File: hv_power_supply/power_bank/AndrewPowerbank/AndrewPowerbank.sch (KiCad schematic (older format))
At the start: 49 parts, among them J1 NanoFit_RA_TH_02, J2 NanoFit_RA_TH_02, J3 USB-A-S-X-X-SM2, J4 USB-Micro-1981568-1, J5 NanoFit_RA_TH_02, Q1 SSM3K333R, U1 MCP73871T-2CCI_ML, U2 TPS61090RSAR

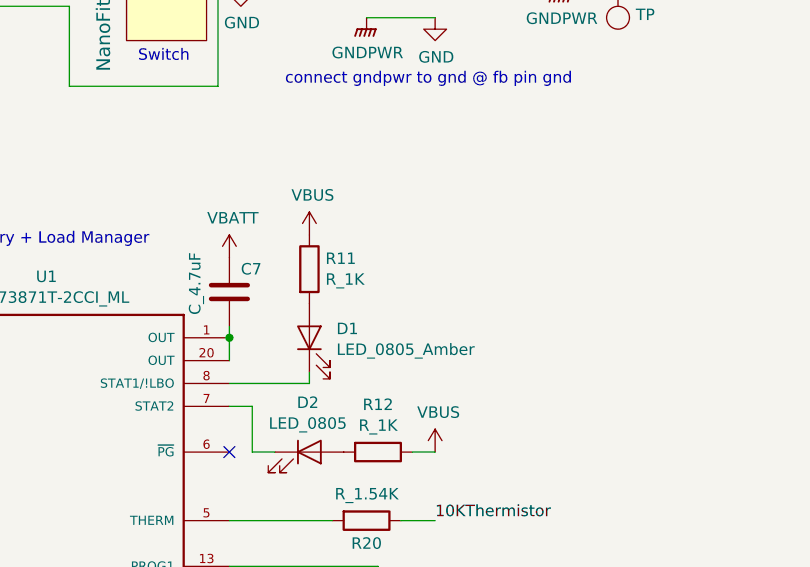
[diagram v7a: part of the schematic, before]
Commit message: Refill GND plane, fix C7 connection.
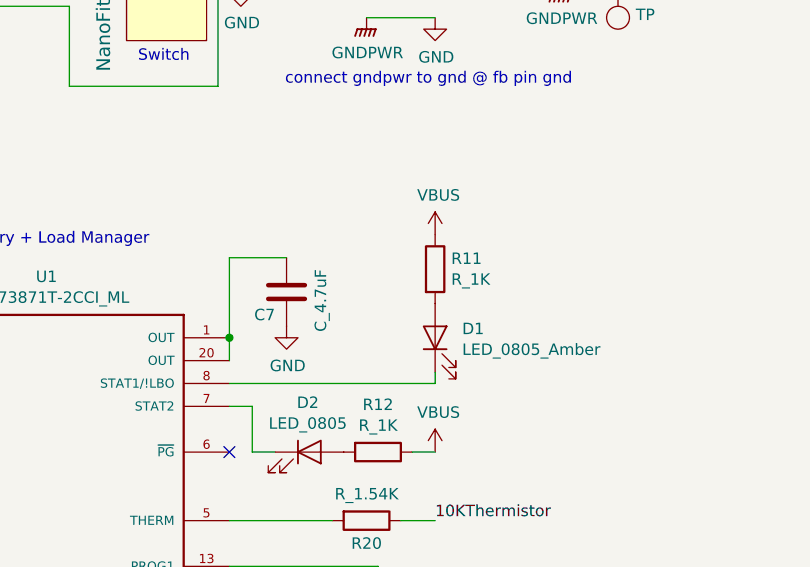
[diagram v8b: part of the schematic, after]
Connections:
- net +BATT: no longer C7.2
- net GND: now also C7.2
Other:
- moved on the sheet: C7, D1, R11
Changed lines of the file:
@@
 L formula:LED_0805_Amber D1
 U 1 1 5FD0F03B
-P 5950 4900
-F 0 "D1" V 5989 4782 50  0000 R CNN
-F 1 "LED_0805_Amber" V 5898 4782 50  0000 R CNN
-F 2 "footprints:LED_0805_OEM" H 5850 4900 50  0001 C CNN
-F 3 "https://media.digikey.com/pdf/Data%20Sheets/Chicago%20Miniature%20Lamps%20PDFs/CMDA5_Series_Rev_Aug_2014.pdf" H 5950 5000 50  0001 C CNN
-F 4 "DK" H 5950 4900 60  0001 C CNN "MFN"
-F 5 "L71517CT-ND" H 5950 4900 60  0001 C CNN "MPN"
-F 6 "https://www.digikey.com/product-detail/en/visual-communications-company-vcc/CMDA5DY7D1S/L71517CT-ND/614867" H 6350 5400 60  0001 C CNN "PurchasingLink"
-	1    5950 4900
+P 6500 4900
+F 0 "D1" V 6539 4782 50  0000 R CNN
+F 1 "LED_0805_Amber" V 6448 4782 50  0000 R CNN
+F 2 "footprints:LED_0805_OEM" H 6400 4900 50  0001 C CNN
+F 3 "https://media.digikey.com/pdf/Data%20Sheets/Chicago%20Miniature%20Lamps%20PDFs/CMDA5_Series_Rev_Aug_2014.pdf" H 6500 5000 50  0001 C CNN
+F 4 "DK" H 6500 4900 60  0001 C CNN "MFN"
+F 5 "L71517CT-ND" H 6500 4900 60  0001 C CNN "MPN"
+F 6 "https://www.digikey.com/product-detail/en/visual-communications-company-vcc/CMDA5DY7D1S/L71517CT-ND/614867" H 6900 5400 60  0001 C CNN "PurchasingLink"
+	1    6500 4900
 	0    -1   -1   0
 $EndComp
@@
 L formula:R_1K R11
 U 1 1 5FD11BE4
-P 5950 4600
-F 0 "R11" H 6020 4646 50  0000 L CNN
-F 1 "R_1K" H 6020 4555 50  0000 L CNN
-F 2 "footprints:R_0805_OEM" H 5880 4600 50  0001 C CNN
-F 3 "https://www.seielect.com/Catalog/SEI-rncp.pdf" H 6030 4600 50  0001 C CNN
-F 4 "DK" H 5950 4600 60  0001 C CNN "MFN"
-F 5 "RNCP0805FTD1K00CT-ND" H 5950 4600 60  0001 C CNN "MPN"
-F 6 "https://www.digikey.com/products/en?keywords=RNCP0805FTD1K00CT-ND" H 6430 5000 60  0001 C CNN "PurchasingLink"
-	1    5950 4600
+P 6500 4600
+F 0 "R11" H 6570 4646 50  0000 L CNN
+F 1 "R_1K" H 6570 4555 50  0000 L CNN
+F 2 "footprints:R_0805_OEM" H 6430 4600 50  0001 C CNN
+F 3 "https://www.seielect.com/Catalog/SEI-rncp.pdf" H 6580 4600 50  0001 C CNN
+F 4 "DK" H 6500 4600 60  0001 C CNN "MFN"
+F 5 "RNCP0805FTD1K00CT-ND" H 6500 4600 60  0001 C CNN "MPN"
+F 6 "https://www.digikey.com/products/en?keywords=RNCP0805FTD1K00CT-ND" H 6980 5000 60  0001 C CNN "PurchasingLink"
+	1    6500 4600
 	1    0    0    -1
 $EndComp
@@
 	8600 2050 8950 2050
 Wire Wire Line
-	5950 5100 5950 5050
+	6500 5100 6500 5050
 $Comp
 L formula:MCP73871T-2CCI_ML U1
@@
 L power:VBUS #PWR026
 U 1 1 60347B3B
-P 5950 4450
-F 0 "#PWR026" H 5950 4300 50  0001 C CNN
-F 1 "VBUS" H 5965 4623 50  0000 C CNN
-F 2 "" H 5950 4450 50  0001 C CNN
-F 3 "" H 5950 4450 50  0001 C CNN
-	1    5950 4450
+P 6500 4450
+F 0 "#PWR026" H 6500 4300 50  0001 C CNN
+F 1 "VBUS" H 6515 4623 50  0000 C CNN
+F 2 "" H 6500 4450 50  0001 C CNN
+F 3 "" H 6500 4450 50  0001 C CNN
+	1    6500 4450
 	1    0    0    -1
 $EndComp
@@
 Wire Wire Line
 	5600 5700 6050 5700
-Wire Wire Line
-	5600 5100 5950 5100
 Wire Wire Line
 	4000 6000 4000 5900
@@
 	1    0    0    -1
 $EndComp
-Wire Wire Line
-	5600 4850 5600 4900
-$Comp
-L formula:VBATT #PWR023
-U 1 1 5FD0E8DA
-P 5600 4550
-F 0 "#PWR023" H 5600 4400 50  0001 C CNN
-F 1 "VBATT" H 5615 4723 50  0000 C CNN
-F 2 "" H 5600 4550 50  0001 C CNN
-F 3 "" H 5600 4550 50  0001 C CNN
-	1    5600 4550
-	1    0    0    -1
-$EndComp
 $Comp
 L formula:C_4.7uF C7
 U 1 1 602FB6FA
-P 5600 4700
-F 0 "C7" H 5550 4600 50  0000 R CNN
-F 1 "C_4.7uF" V 5750 4800 50  0000 R CNN
-F 2 "footprints:C_0603_1608Metric" H 5638 4550 50  0001 C CNN
-F 3 "http://www.samsungsem.com/kr/support/product-search/mlcc/CL10A475KQ8NNNC.jsp" H 5625 4800 50  0001 C CNN
-F 4 "DK" H 5600 4700 60  0001 C CNN "MFN"
-F 5 "1276-1045-1-ND" H 5600 4700 60  0001 C CNN "MPN"
-F 6 "https://www.digikey.com/product-detail/en/samsung-electro-mechanics/CL10A475KQ8NNNC/1276-1045-1-ND/3889131" H 6025 5200 60  0001 C CNN "PurchasingLink"
-	1    5600 4700
-	-1   0    0    1
+P 5850 4700
+F 0 "C7" H 5800 4600 50  0000 R CNN
+F 1 "C_4.7uF" V 6000 4800 50  0000 R CNN
+F 2 "footprints:C_0603_1608Metric" H 5888 4550 50  0001 C CNN
+F 3 "http://www.samsungsem.com/kr/support/product-search/mlcc/CL10A475KQ8NNNC.jsp" H 5875 4800 50  0001 C CNN
+F 4 "DK" H 5850 4700 60  0001 C CNN "MFN"
+F 5 "1276-1045-1-ND" H 5850 4700 60  0001 C CNN "MPN"
+F 6 "https://www.digikey.com/product-detail/en/samsung-electro-mechanics/CL10A475KQ8NNNC/1276-1045-1-ND/3889131" H 6275 5200 60  0001 C CNN "PurchasingLink"
+	1    5850 4700
+	1    0    0    -1
 $EndComp
 $Comp
@@
 	1    0    0    -1
 $EndComp
+Wire Wire Line
+	5600 5100 6500 5100
+Wire Wire Line
+	5600 4550 5850 4550
+$Comp
+L power:GND #PWR?
+U 1 1 607436CF
+P 5850 4850
+F 0 "#PWR?" H 5850 4600 50  0001 C CNN
+F 1 "GND" H 5855 4677 50  0000 C CNN
+F 2 "" H 5850 4850 50  0001 C CNN
+F 3 "" H 5850 4850 50  0001 C CNN
+	1    5850 4850
+	1    0    0    -1
+$EndComp
+Wire Wire Line
+	5600 4550 5600 4900
 $EndSCHEMATC
